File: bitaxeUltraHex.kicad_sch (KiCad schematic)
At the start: 12 parts, among them J1 Conn_01x01, J2 Conn_01x01

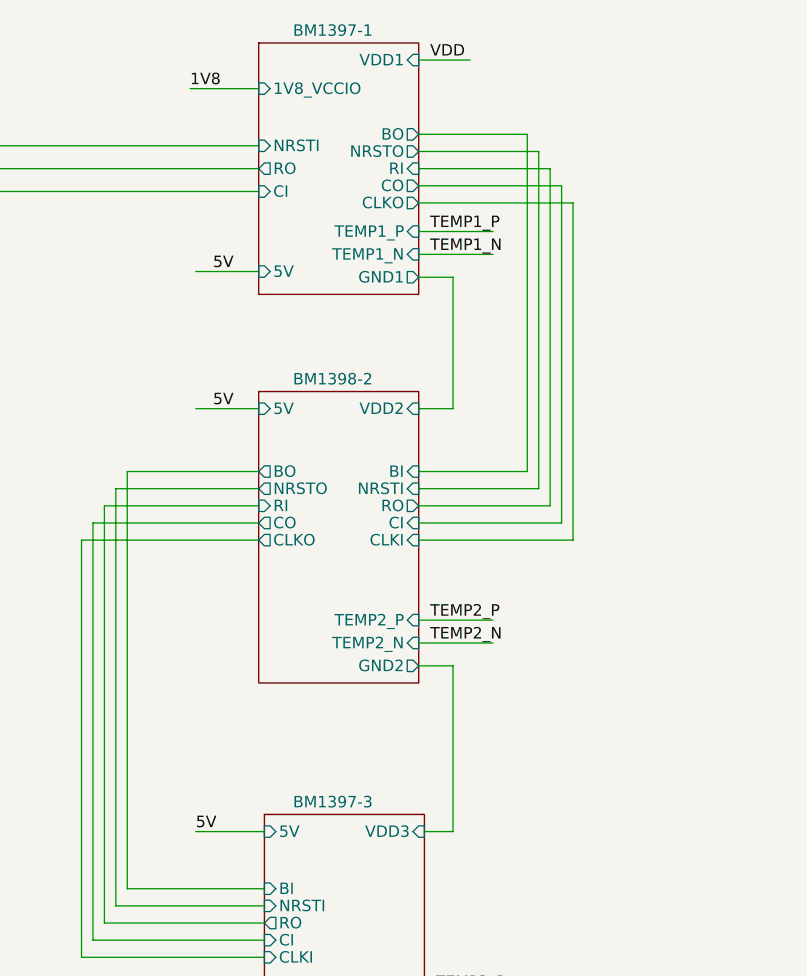
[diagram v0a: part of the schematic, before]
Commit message: update with BM1366
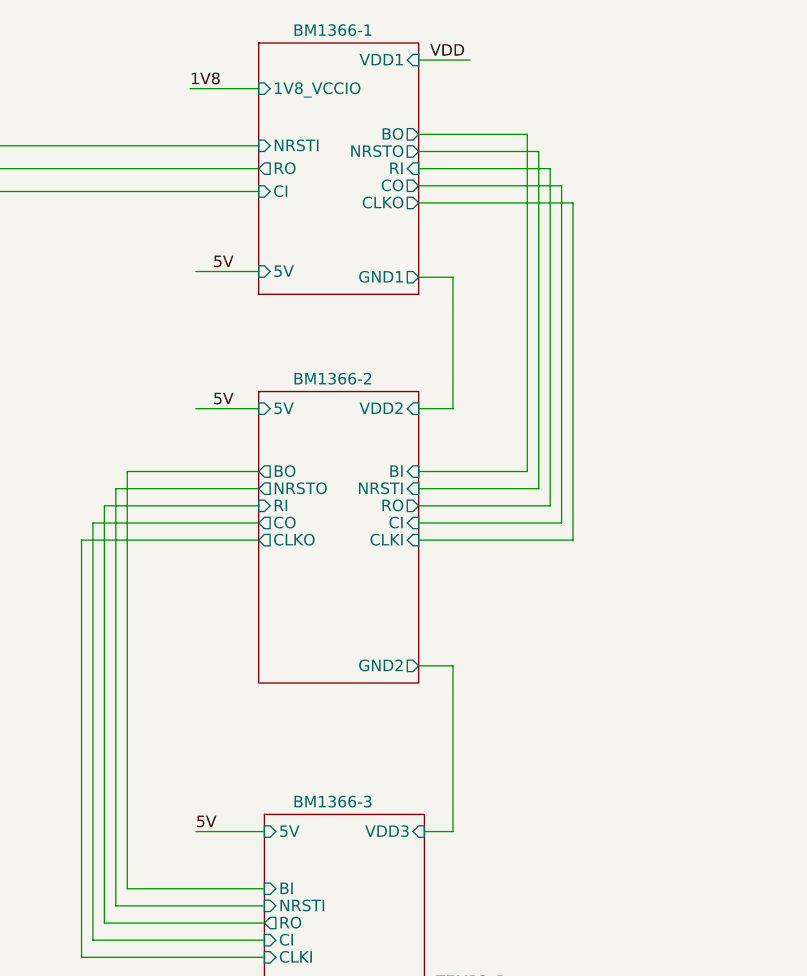
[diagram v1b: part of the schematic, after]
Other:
- sheet BM1397-1 renamed BM1366-1
- sheet BM1397-3 renamed BM1366-3
- sheet BM1398-2 renamed BM1366-2
- sheet BM1366-1: file bm1397-1.kicad_sch -> bm1366-1.kicad_sch
- sheet BM1366-1 ports: added none; removed TEMP1_N, TEMP1_P
- sheet BM1366-2: file bm1397-2.kicad_sch -> bm1366-2.kicad_sch
- sheet BM1366-2 ports: added none; removed TEMP2_N, TEMP2_P
- sheet BM1366-3: file bm1397-3.kicad_sch -> bm1366-3.kicad_sch
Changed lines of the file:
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@@
-    (stroke (width 0) (type default))
-  )
-  (wire (pts (xy 168.91 49.53) (xy 177.165 49.53))
     (stroke (width 0) (type default))
   )
@@
     (stroke (width 0) (type default))
   )
-  (wire (pts (xy 168.91 95.25) (xy 177.165 95.25))
-    (stroke (width 0) (type default))
-  )
   (wire (pts (xy 133.985 126.365) (xy 151.765 126.365))
     (stroke (width 0) (type default))
@@
     (stroke (width 0) (type default))
   )
-  (wire (pts (xy 168.91 92.71) (xy 177.165 92.71))
-    (stroke (width 0) (type default))
-  )
   (wire (pts (xy 180.975 76.2) (xy 168.91 76.2))
     (stroke (width 0) (type default))
@@
     (stroke (width 0) (type default))
   )
-  (wire (pts (xy 168.91 52.07) (xy 177.165 52.07))
-    (stroke (width 0) (type default))
-  )
   (wire (pts (xy 186.055 46.355) (xy 186.055 83.82))
     (stroke (width 0) (type default))
@@
     (effects (font (size 1.27 1.27)) (justify left bottom))
   )
-  (label "TEMP1_P" (at 170.18 49.53 0) (fields_autoplaced)
-    (effects (font (size 1.27 1.27)) (justify left bottom))
-  )
   (label "1V8" (at 61.595 88.265 0) (fields_autoplaced)
     (effects (font (size 1.27 1.27)) (justify left bottom))
@@
     (effects (font (size 1.27 1.27)) (justify left bottom))
   )
-  (label "TEMP2_P" (at 170.18 92.71 0) (fields_autoplaced)
-    (effects (font (size 1.27 1.27)) (justify left bottom))
-  )
   (label "TEMP3_P" (at 170.815 133.985 0) (fields_autoplaced)
     (effects (font (size 1.27 1.27)) (justify left bottom))
@@
     (effects (font (size 1.27 1.27)) (justify left bottom))
   )
-  (label "TEMP2_N" (at 170.18 95.25 0) (fields_autoplaced)
-    (effects (font (size 1.27 1.27)) (justify left bottom))
-  )
   (label "3V3" (at 95.25 38.735 0) (fields_autoplaced)
     (effects (font (size 1.27 1.27)) (justify left bottom))
   )
   (label "3V3" (at 61.595 73.66 0) (fields_autoplaced)
-    (effects (font (size 1.27 1.27)) (justify left bottom))
-  )
-  (label "TEMP1_N" (at 170.18 52.07 0) (fields_autoplaced)
     (effects (font (size 1.27 1.27)) (justify left bottom))
   )
@@
     (pin "1")
     (instances
-      (project "bitaxeHex"
+      (project "bitaxeUltraHex"
         (path "/e63e39d7-6ac0-4ffd-8aa3-1841a4541b55"
           (reference "J1") (unit 1)
@@
     )
     (instances
-      (project "bitaxeHex"
+      (project "bitaxeUltraHex"
         (path "/e63e39d7-6ac0-4ffd-8aa3-1841a4541b55"
           (reference "H3") (unit 1)
@@
     )
     (instances
-      (project "bitaxeHex"
+      (project "bitaxeUltraHex"
         (path "/e63e39d7-6ac0-4ffd-8aa3-1841a4541b55"
           (reference "H7") (unit 1)
@@
     )
     (instances
-      (project "bitaxeHex"
+      (project "bitaxeUltraHex"
         (path "/e63e39d7-6ac0-4ffd-8aa3-1841a4541b55"
           (reference "H10") (unit 1)
@@
     )
     (instances
-      (project "bitaxeHex"
+      (project "bitaxeUltraHex"
         (path "/e63e39d7-6ac0-4ffd-8aa3-1841a4541b55"
           (reference "H8") (unit 1)
@@
     )
     (instances
-      (project "bitaxeHex"
+      (project "bitaxeUltraHex"
         (path "/e63e39d7-6ac0-4ffd-8aa3-1841a4541b55"
           (reference "#G1") (unit 1)
@@
     )
     (instances
-      (project "bitaxeHex"
+      (project "bitaxeUltraHex"
         (path "/e63e39d7-6ac0-4ffd-8aa3-1841a4541b55"
           (reference "H2") (unit 1)
@@
     (pin "1")
     (instances
-      (project "bitaxeHex"
+      (project "bitaxeUltraHex"
         (path "/e63e39d7-6ac0-4ffd-8aa3-1841a4541b55"
           (reference "J2") (unit 1)
@@
     )
     (instances
-      (project "bitaxeHex"
+      (project "bitaxeUltraHex"
         (path "/e63e39d7-6ac0-4ffd-8aa3-1841a4541b55"
           (reference "H1") (unit 1)
@@
     )
     (instances
-      (project "bitaxeHex"
+      (project "bitaxeUltraHex"
         (path "/e63e39d7-6ac0-4ffd-8aa3-1841a4541b55"
           (reference "H6") (unit 1)
@@
     )
     (instances
-      (project "bitaxeHex"
+      (project "bitaxeUltraHex"
         (path "/e63e39d7-6ac0-4ffd-8aa3-1841a4541b55"
           (reference "H5") (unit 1)
@@
     )
     (instances
-      (project "bitaxeHex"
+      (project "bitaxeUltraHex"
         (path "/e63e39d7-6ac0-4ffd-8aa3-1841a4541b55"
           (reference "H9") (unit 1)
@@
     )
     (instances
-      (project "bitaxeHex"
+      (project "bitaxeUltraHex"
         (path "/e63e39d7-6ac0-4ffd-8aa3-1841a4541b55"
           (reference "H4") (unit 1)
@@
     (stroke (width 0.1524) (type solid))
     (fill (color 255 255 194 1.0000))
-    (property "Sheetname" "BM1397-1" (at 154.94 27.94 0)
+    (property "Sheetname" "BM1366-1" (at 154.94 27.94 0)
       (effects (font (size 1.27 1.27)) (justify left bottom))
     )
-    (property "Sheetfile" "bm1397-1.kicad_sch" (at 150.495 58.42 0)
+    (property "Sheetfile" "bm1366-1.kicad_sch" (at 150.495 58.42 0)
       (effects (font (size 1.27 1.27)) (justify left top) hide)
     )
@@
       (effects (font (size 1.27 1.27)) (justify right))
     )
-    (pin "TEMP1_N" input (at 168.91 52.07 0)
-      (effects (font (size 1.27 1.27)) (justify right))
-    )
-    (pin "TEMP1_P" input (at 168.91 49.53 0)
-      (effects (font (size 1.27 1.27)) (justify right))
-    )
     (pin "1V8_VCCIO" input (at 151.13 33.655 180)
       (effects (font (size 1.27 1.27)) (justify left))
     )
     (instances
-      (project "bitaxeHex"
+      (project "bitaxeUltraHex"
         (path "/e63e39d7-6ac0-4ffd-8aa3-1841a4541b55" (page "4"))
       )
@@
     (stroke (width 0.1524) (type solid))
     (fill (color 255 255 194 1.0000))
-    (property "Sheetname" "BM1398-2" (at 154.94 66.675 0)
+    (property "Sheetname" "BM1366-2" (at 154.94 66.675 0)
       (effects (font (size 1.27 1.27)) (justify left bottom))
     )
-    (property "Sheetfile" "bm1397-2.kicad_sch" (at 151.13 103.4546 0)
+    (property "Sheetfile" "bm1366-2.kicad_sch" (at 151.13 103.4546 0)
       (effects (font (size 1.27 1.27)) (justify left top) hide)
     )
@@
       (effects (font (size 1.27 1.27)) (justify left))
     )
-    (pin "TEMP2_N" input (at 168.91 95.25 0)
-      (effects (font (size 1.27 1.27)) (justify right))
-    )
-    (pin "TEMP2_P" input (at 168.91 92.71 0)
-      (effects (font (size 1.27 1.27)) (justify right))
-    )
-    (instances
-      (project "bitaxeHex"
+    (instances
+      (project "bitaxeUltraHex"
         (path "/e63e39d7-6ac0-4ffd-8aa3-1841a4541b55" (page "6"))
       )
@@
     )
     (instances
-      (project "bitaxeHex"
+      (project "bitaxeUltraHex"
         (path "/e63e39d7-6ac0-4ffd-8aa3-1841a4541b55" (page "5"))
       )
@@
     )
     (instances
-      (project "bitaxeHex"
+      (project "bitaxeUltraHex"
         (path "/e63e39d7-6ac0-4ffd-8aa3-1841a4541b55" (page "2"))
       )
@@
     )
     (instances
-      (project "bitaxeHex"
+      (project "bitaxeUltraHex"
         (path "/e63e39d7-6ac0-4ffd-8aa3-1841a4541b55" (page "3"))
       )
@@
     (stroke (width 0.1524) (type solid))
     (fill (color 255 255 194 1.0000))
-    (property "Sheetname" "BM1397-3" (at 154.94 113.665 0)
+    (property "Sheetname" "BM1366-3" (at 154.94 113.665 0)
       (effects (font (size 1.27 1.27)) (justify left bottom))
     )
-    (property "Sheetfile" "bm1397-3.kicad_sch" (at 151.765 141.5546 0)
+    (property "Sheetfile" "bm1366-3.kicad_sch" (at 151.765 141.5546 0)
       (effects (font (size 1.27 1.27)) (justify left top) hide)
     )
@@
     )
     (instances
-      (project "bitaxeHex"
+      (project "bitaxeUltraHex"
         (path "/e63e39d7-6ac0-4ffd-8aa3-1841a4541b55" (page "7"))
       )
